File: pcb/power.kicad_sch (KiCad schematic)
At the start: 21 parts, among them J1 9V Battery, J2 9V Barrel Female

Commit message: First revision of the pcb layout
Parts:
- C? (x3): footprint Capacitor_SMD:C_1206_3216Metric -> Capacitor_SMD:C_0402_1005Metric; LCSC C577121 -> C1525; MPN CC1206JKNPO9BN104 -> CL05B104KO5NNNC; Manufacturer Yageo -> Samsung Electro-Mechanics
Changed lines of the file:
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@@
       (effects (font (size 1.27 1.27)))
     )
-    (property "Footprint" "Capacitor_SMD:C_1206_3216Metric" (at 236.22 116.84 0)
+    (property "Footprint" "Capacitor_SMD:C_0402_1005Metric" (at 236.22 116.84 0)
       (effects (font (size 1.27 1.27)) hide)
     )
@@
       (effects (font (size 1.27 1.27)) hide)
     )
-    (property "LCSC" "C577121" (at 236.22 116.84 0)
+    (property "LCSC" "C1525" (at 236.22 116.84 0)
       (effects (font (size 1.27 1.27)) hide)
     )
-    (property "MPN" "CC1206JKNPO9BN104" (at 236.22 116.84 0)
+    (property "MPN" "CL05B104KO5NNNC" (at 236.22 116.84 0)
       (effects (font (size 1.27 1.27)) hide)
     )
-    (property "Manufacturer" "Yageo" (at 236.22 116.84 0)
+    (property "Manufacturer" "Samsung Electro-Mechanics" (at 236.22 116.84 0)
       (effects (font (size 1.27 1.27)) hide)
     )
@@
       (effects (font (size 1.27 1.27)))
     )
-    (property "Footprint" "Capacitor_SMD:C_1206_3216Metric" (at 114.3 83.82 0)
+    (property "Footprint" "Capacitor_SMD:C_0402_1005Metric" (at 114.3 83.82 0)
       (effects (font (size 1.27 1.27)) hide)
     )
@@
       (effects (font (size 1.27 1.27)) hide)
     )
-    (property "LCSC" "C577121" (at 114.3 83.82 0)
+    (property "LCSC" "C1525" (at 114.3 83.82 0)
       (effects (font (size 1.27 1.27)) hide)
     )
-    (property "MPN" "CC1206JKNPO9BN104" (at 114.3 83.82 0)
+    (property "MPN" "CL05B104KO5NNNC" (at 114.3 83.82 0)
       (effects (font (size 1.27 1.27)) hide)
     )
-    (property "Manufacturer" "Yageo" (at 114.3 83.82 0)
+    (property "Manufacturer" "Samsung Electro-Mechanics" (at 114.3 83.82 0)
       (effects (font (size 1.27 1.27)) hide)
     )
@@
       (effects (font (size 1.27 1.27)))
     )
-    (property "Footprint" "Capacitor_SMD:C_1206_3216Metric" (at 71.12 86.36 0)
+    (property "Footprint" "Capacitor_SMD:C_0402_1005Metric" (at 71.12 86.36 0)
       (effects (font (size 1.27 1.27)) hide)
     )
@@
       (effects (font (size 1.27 1.27)) hide)
     )
-    (property "LCSC" "C577121" (at 71.12 86.36 0)
+    (property "LCSC" "C1525" (at 71.12 86.36 0)
       (effects (font (size 1.27 1.27)) hide)
     )
-    (property "MPN" "CC1206JKNPO9BN104" (at 71.12 86.36 0)
+    (property "MPN" "CL05B104KO5NNNC" (at 71.12 86.36 0)
       (effects (font (size 1.27 1.27)) hide)
     )
-    (property "Manufacturer" "Yageo" (at 71.12 86.36 0)
+    (property "Manufacturer" "Samsung Electro-Mechanics" (at 71.12 86.36 0)
       (effects (font (size 1.27 1.27)) hide)
     )

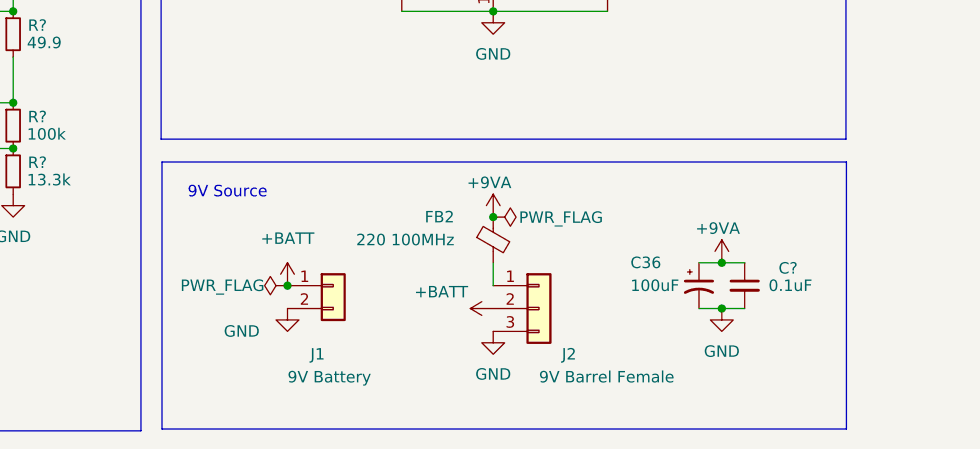
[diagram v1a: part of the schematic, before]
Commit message: Lowered resistor values and added protection diode
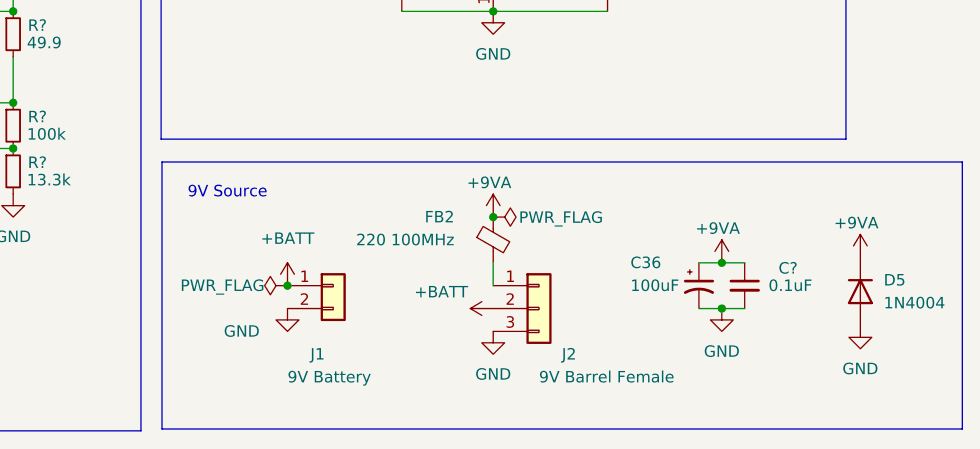
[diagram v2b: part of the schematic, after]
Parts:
- added D5: 1N4004, Diode_THT:D_DO-41_SOD81_P10.16mm_Horizontal, symbol Diode:1N4004
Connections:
- net +9VA: now also D5.1 (K)
- net GND: now also D5.2 (A)
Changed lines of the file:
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@@
     (fill (type none))
   )
-  (rectangle (start 171.4754 103.0986) (end 247.523 132.7658)
+  (rectangle (start 171.4754 103.0986) (end 260.4008 132.7658)
     (stroke (width 0) (type default))
     (fill (type none))
@@
     )
   )
+  (symbol (lib_id "power:GND") (at 249.0724 121.3104 0) (unit 1)
+    (in_bom yes) (on_board yes) (dnp no) (fields_autoplaced)
+    (property "Reference" "#PWR066" (at 249.0724 127.6604 0)
+      (effects (font (size 1.27 1.27)) hide)
+    )
+    (property "Value" "GND" (at 249.0724 126.0856 0)
+      (effects (font (size 1.27 1.27)))
+    )
+    (property "Footprint" "" (at 249.0724 121.3104 0)
+      (effects (font (size 1.27 1.27)) hide)
+    )
+    (property "Datasheet" "" (at 249.0724 121.3104 0)
+      (effects (font (size 1.27 1.27)) hide)
+    )
+    (pin "1")
+    (instances
+      (project "tuner_pedal"
+        (path "/be09f3cc-c79c-49de-93a4-4a01bf6bfbcf/9ea77ce1-53e9-4640-bd59-4fc38cd754df"
+          (reference "#PWR066") (unit 1)
+        )
+      )
+    )
+  )
   (symbol (lib_id "Device:C_Small") (at 236.22 116.84 0) (unit 1)
     (in_bom yes) (on_board yes) (dnp no)
@@
     )
   )
+  (symbol (lib_id "power:+9VA") (at 249.0724 113.6904 0) (unit 1)
+    (in_bom yes) (on_board yes) (dnp no)
+    (property "Reference" "#PWR065" (at 249.0724 116.8654 0)
+      (effects (font (size 1.27 1.27)) hide)
+    )
+    (property "Value" "+9VA" (at 248.6152 109.8804 0)
+      (effects (font (size 1.27 1.27)))
+    )
+    (property "Footprint" "" (at 249.0724 113.6904 0)
+      (effects (font (size 1.27 1.27)) hide)
+    )
+    (property "Datasheet" "" (at 249.0724 113.6904 0)
+      (effects (font (size 1.27 1.27)) hide)
+    )
+    (pin "1")
+    (instances
+      (project "tuner_pedal"
+        (path "/be09f3cc-c79c-49de-93a4-4a01bf6bfbcf/9ea77ce1-53e9-4640-bd59-4fc38cd754df"
+          (reference "#PWR065") (unit 1)
+        )
+      )
+    )
+  )
   (symbol (lib_id "power:+9VA") (at 66.04 81.28 0) (unit 1)
     (in_bom yes) (on_board yes) (dnp no) (fields_autoplaced)
@@
         )
       )
+    )
+  )
+  (symbol (lib_id "Diode:1N4004") (at 249.0724 117.5004 270) (unit 1)
+    (in_bom yes) (on_board yes) (dnp no) (fields_autoplaced)
+    (property "Reference" "D5" (at 251.6632 116.2304 90)
+      (effects (font (size 1.27 1.27)) (justify left))
+    )
+    (property "Value" "1N4004" (at 251.6632 118.7704 90)
+      (effects (font (size 1.27 1.27)) (justify left))
+    )
+    (property "Footprint" "Diode_THT:D_DO-41_SOD81_P10.16mm_Horizontal" (at 244.6274 117.5004 0)
+      (effects (font (size 1.27 1.27)) hide)
+    )
+    (property "Datasheet" "http://www.vishay.com/docs/88503/1n4001.pdf" (at 249.0724 117.5004 0)
+      (effects (font (size 1.27 1.27)) hide)
+    )
+    (property "Sim.Device" "D" (at 249.0724 117.5004 0)
+      (effects (font (size 1.27 1.27)) hide)
+    )
+    (property "Sim.Pins" "1=K 2=A" (at 249.0724 117.5004 0)
+      (effects (font (size 1.27 1.27)) hide)
+    )
+    (property "LCSC" "C3058" (at 249.0724 117.5004 0)
+      (effects (font (size 1.27 1.27)) hide)
+    )
+    (property "MPN" "1N4004" (at 249.0724 117.5004 0)
+      (effects (font (size 1.27 1.27)) hide)
+    )
+    (property "Manufacturer" "MDD (Microdiode Semiconductor)" (at 249.0724 117.5004 0)
+      (effects (font (size 1.27 1.27)) hide)
+    )
+    (pin "1")
+    (pin "2")
+    (instances
+      (project "tuner_pedal"
+        (path "/be09f3cc-c79c-49de-93a4-4a01bf6bfbcf/9ea77ce1-53e9-4640-bd59-4fc38cd754df"
+          (reference "D5") (unit 1)
+        )
+      )
